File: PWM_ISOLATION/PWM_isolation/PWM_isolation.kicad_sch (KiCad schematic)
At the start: 35 parts, among them J1 Conn_01x02_Socket, J10 XT60_Male, J11 Conn_01x03_Pin, J12 Conn_01x02_Socket, J2 Conn_01x02_Socket, J3 Conn_01x02_Socket, J4 Conn_01x02_Socket, J5 Conn_01x05_Socket, J6 Conn_01x03_Socket, J7 Conn_01x03_Socket, J8 Conn_01x03_Socket, J9 Conn_01x03_Socket, U1 TBD62783A, U2 LTV-847

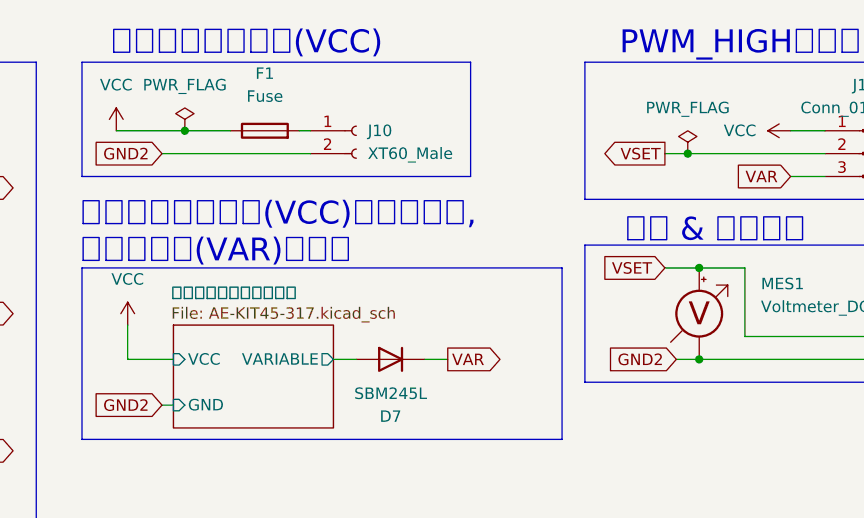
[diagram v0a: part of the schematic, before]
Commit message: CREATE gerber file for PWM_ISOLATION_CIRCUIT
PWM_ISOLATION_CIRCUITのガーバーファイルを作成
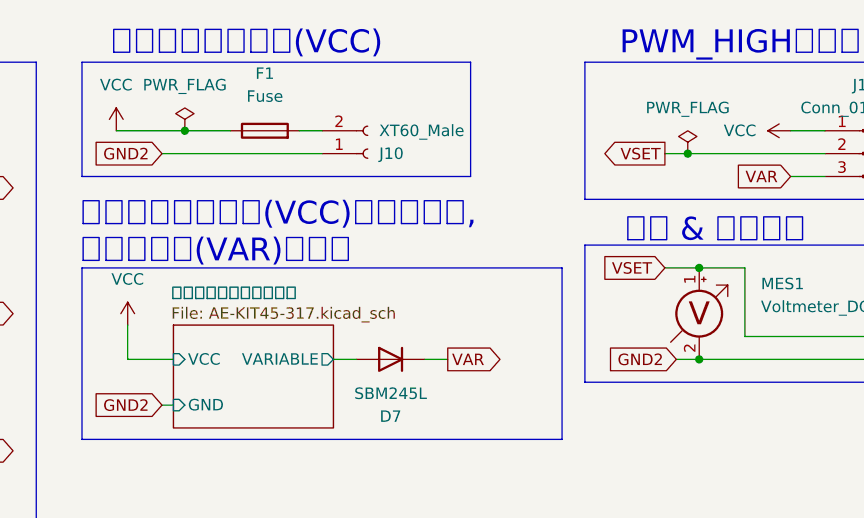
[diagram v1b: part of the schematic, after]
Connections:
- net GND2: now also J10.1 (Pin_1), MES1.2 (-); no longer J10.2 (Pin_2), MES1.1 (-)
- net VSET: now also MES1.1 (+); no longer MES1.2 (+)
- net at F1.2: now also J10.2 (Pin_2); no longer J10.1 (Pin_1)
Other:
- moved on the sheet: J10
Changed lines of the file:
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@@
 	(wire
 		(pts
-			(xy 158.75 38.1) (xy 160.02 38.1)
+			(xy 158.75 38.1) (xy 161.29 38.1)
 		)
 		(stroke
@@
 	(wire
 		(pts
-			(xy 143.51 40.64) (xy 160.02 40.64)
+			(xy 143.51 40.64) (xy 161.29 40.64)
 		)
 		(stroke
@@
 	(symbol
 		(lib_id "Connector:Conn_01x02_Socket")
-		(at 165.1 38.1 0)
+		(at 166.37 40.64 0)
+		(mirror x)
 		(unit 1)
 		(exclude_from_sim no)
@@
 		(dnp no)
 		(property "Reference" "J10"
-			(at 166.37 38.0999 0)
+			(at 167.64 40.6401 0)
 			(effects
 				(font
@@
 		)
 		(property "Value" "XT60_Male"
-			(at 166.37 40.6399 0)
+			(at 167.64 38.1001 0)
 			(effects
 				(font
@@
 		)
 		(property "Footprint" "MyFoot:AMASS_XT60PW-M_1x02_P7.20mm_Horizontal"
-			(at 165.1 38.1 0)
+			(at 166.37 40.64 0)
 			(effects
 				(font
@@
 		)
 		(property "Datasheet" "~"
-			(at 165.1 38.1 0)
+			(at 166.37 40.64 0)
 			(effects
 				(font
@@
 		)
 		(property "Description" "Generic connector, single row, 01x02, script generated"
-			(at 165.1 38.1 0)
-			(effects
-				(font
+			(at 166.37 40.64 0)
+			(effects
+				(font
